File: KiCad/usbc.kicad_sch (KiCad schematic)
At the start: 2 parts, among them J15 JACK-USBE-20PINTL, U9 TPS65987DDKRSHR

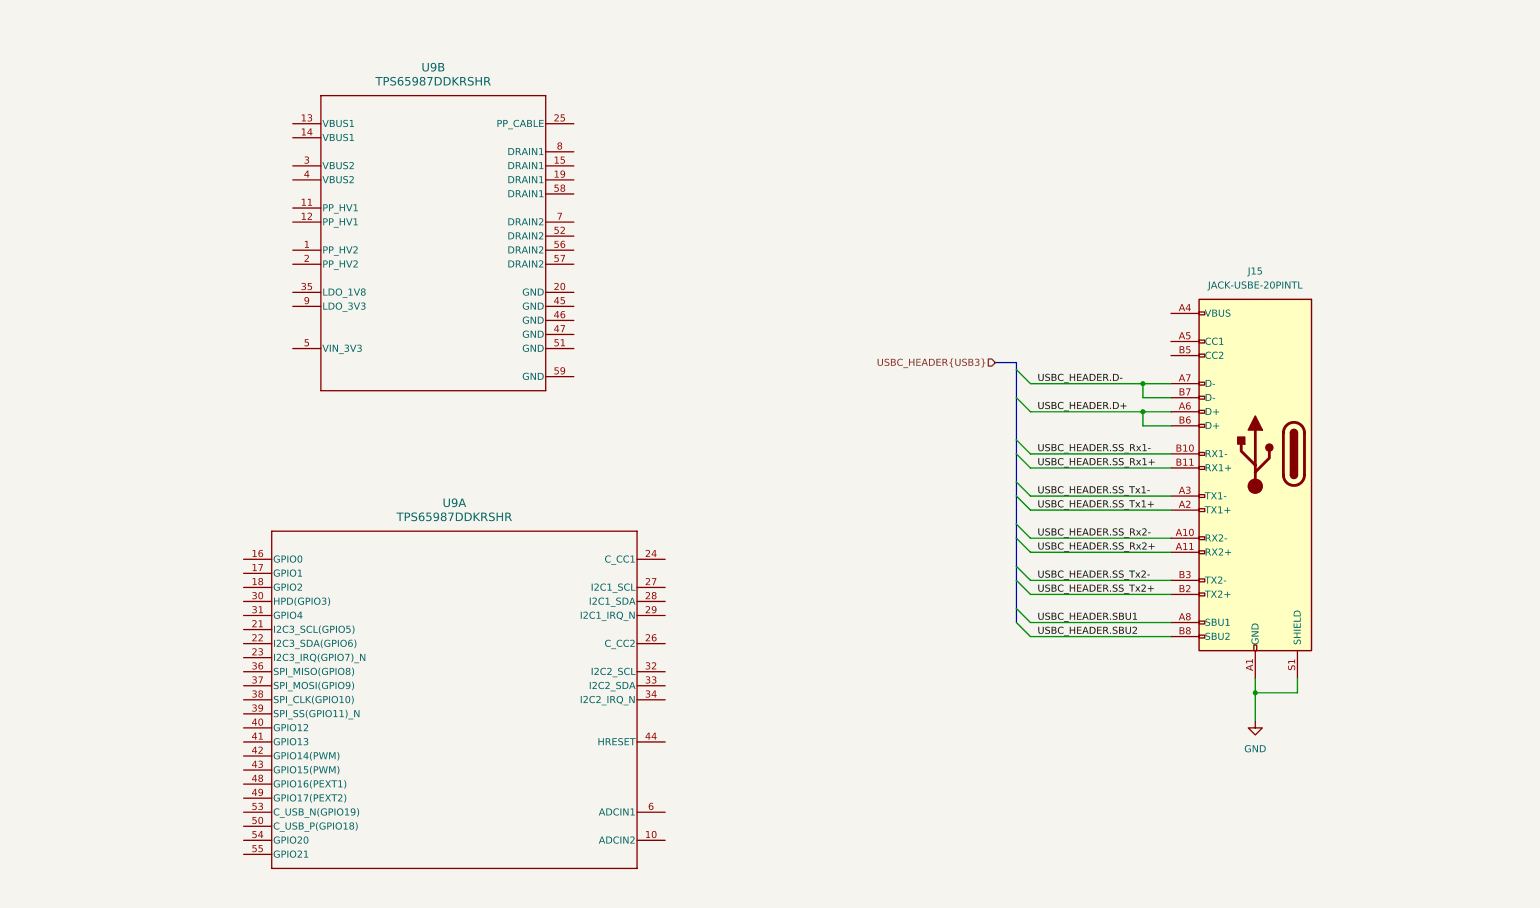
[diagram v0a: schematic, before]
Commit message: Connect TPS65987D I2C and Interrupts
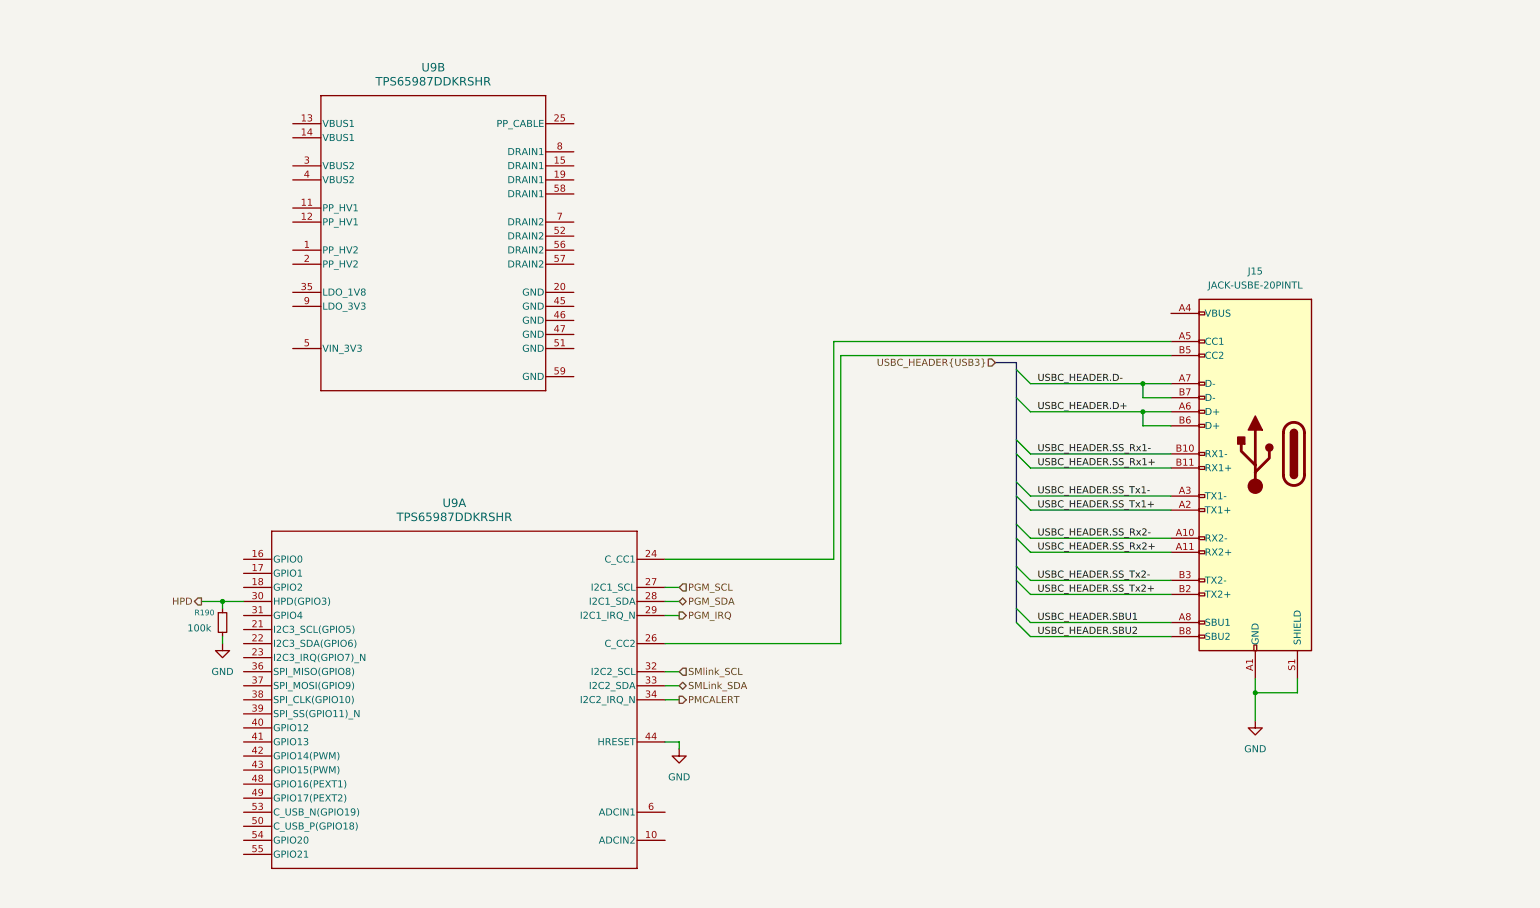
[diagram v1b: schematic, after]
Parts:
- added R190: 100k, symbol Device:R_Small
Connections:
- net GND: now also U9.44 (HRESET), R190.2
- net at J15.A5 (CC1): now also U9.24 (C_CC1)
- net at J15.B5 (CC2): now also U9.26 (C_CC2)
- net PGM_SCL: now reaches U9.27 (I2C1_SCL)
- net PGM_SDA: now reaches U9.28 (I2C1_SDA)
- net PGM_IRQ: now reaches U9.29 (I2C1_IRQ_N)
- net HPD: now reaches U9.30 (HPD(GPIO3))
- net HPD: now also R190.1
- net SMlink_SCL: now reaches U9.32 (I2C2_SCL)
- net SMLink_SDA: now reaches U9.33 (I2C2_SDA)
- net PMCALERT: now reaches U9.34 (I2C2_IRQ_N)

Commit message: Finish wiring TPS65987D
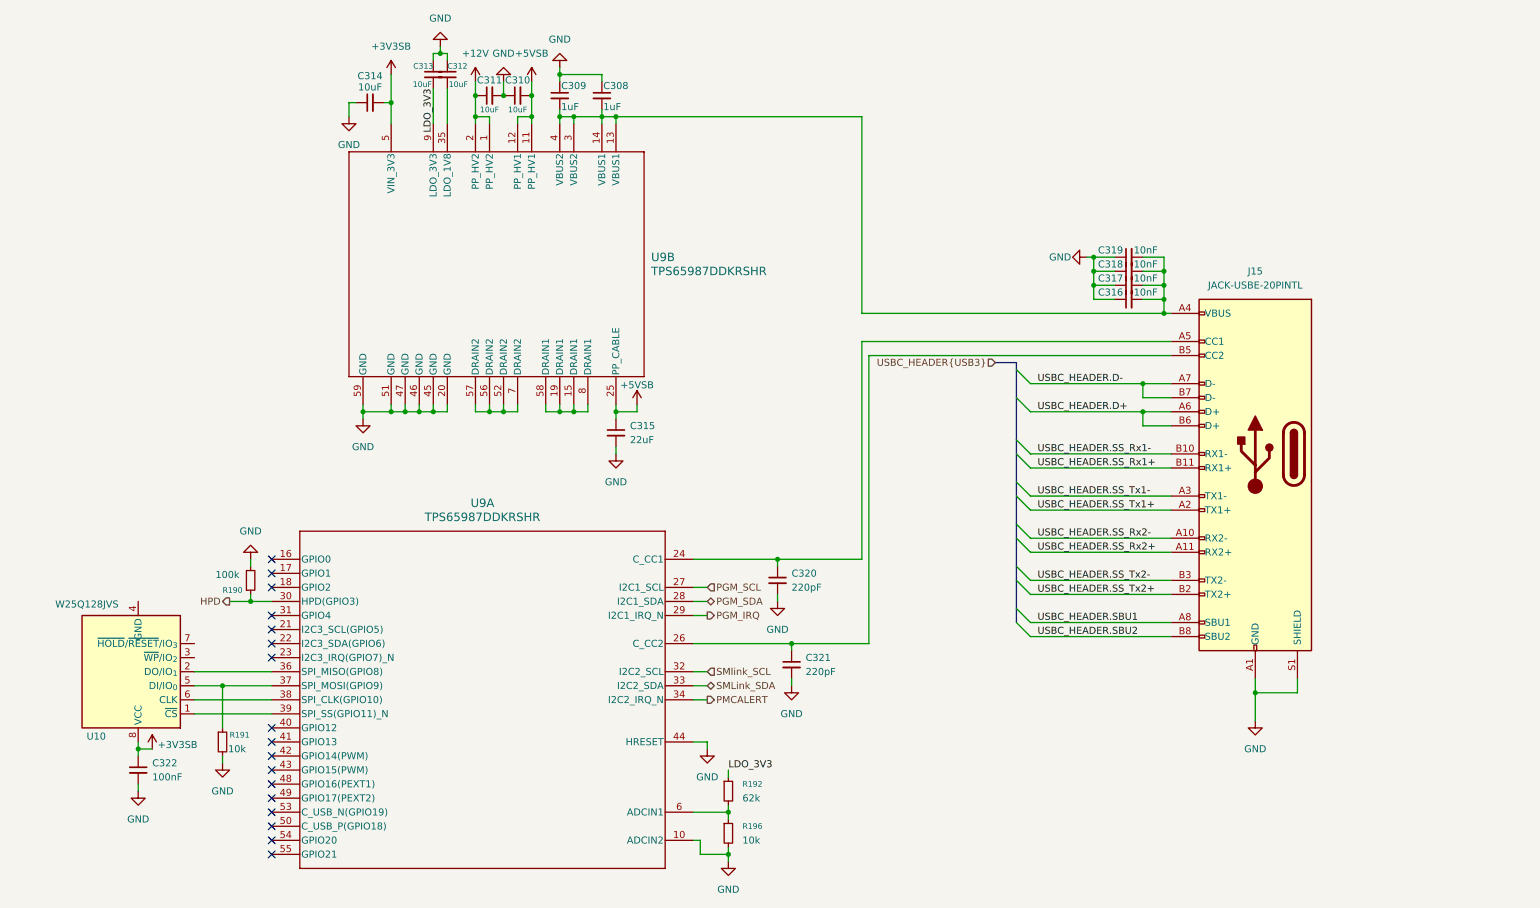
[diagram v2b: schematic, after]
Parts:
- added C308, C309: 1uF, symbol Device:C_Small
- added C310, C311, C312, C313, C314: 10uF, symbol Device:C_Small
- added C315: 22uF, symbol Device:C_Small
- added C316, C317, C318, C319: 10nF, symbol Device:C_Small
- added C320, C321: 220pF, symbol Device:C_Small
- added C322: 100nF, symbol Device:C_Small
- added R191, R196: 10k, symbol Device:R_Small
- added R192: 62k, symbol Device:R_Small
- added U10: W25Q128JVS, Package_SO:SOIC-8_5.3x5.3mm_P1.27mm, symbol Memory_Flash:W25Q128JVS
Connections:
- net GND: now also U9.10 (ADCIN2), U9.20 (GND), U9.45 (GND), U9.46 (GND), U9.47 (GND), U9.51 (GND), U9.59 (GND), C308.1, C309.1, C310.1, C311.2, C312.1, C313.1, C314.1, C315.2, C316.1, C317.1, C318.1, C319.1, C320.2, C321.2, C322.2, R191.2, R196.2
- net at J15.A4 (VBUS), J15.A9 (VBUS), J15.B4 (VBUS)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: now also U9.13 (VBUS1), U9.14 (VBUS1), U9.3 (VBUS2), U9.4 (VBUS2), C308.2, C309.2, C316.2, C317.2, C318.2, C319.2
- net at J15.A5 (CC1), U9.24 (C_CC1): now also C320.1
- net at J15.B5 (CC2), U9.26 (C_CC2): now also C321.1
- net at U9.36 (SPI_MISO(GPIO8)): now also U10.2 (DO/IO_{1})
- net at U9.37 (SPI_MOSI(GPIO9)): now also R191.1, U10.5 (DI/IO_{0})
- net at U9.38 (SPI_CLK(GPIO10)): now also U10.6 (CLK)
- net at U9.39 (SPI_SS(GPIO11)_N): now also U10.1 (~{CS})
- net at U9.6 (ADCIN1): now also R192.2, R196.1
- net +12V: now reaches U9.1 (PP_HV2)
- net +12V: now also U9.2 (PP_HV2), C311.1
- net +5VSB: now reaches U9.11 (PP_HV1)
- net +5VSB: now also U9.12 (PP_HV1), U9.25 (PP_CABLE), C310.2, C315.1
- net at U9.15 (DRAIN1): now also U9.19 (DRAIN1), U9.58 (DRAIN1), U9.8 (DRAIN1)
- net at U9.35 (LDO_1V8): now also C312.2
- net +3V3SB: now reaches U9.5 (VIN_3V3)
- net +3V3SB: now also C314.2, C322.1, U10.8 (VCC)
- net at U9.52 (DRAIN2): now also U9.56 (DRAIN2), U9.57 (DRAIN2), U9.7 (DRAIN2)
- net LDO_3V3: now reaches U9.9 (LDO_3V3)
- net LDO_3V3: now also C313.2, R192.1
- no-connect marks 0 -> 17
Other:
- moved on the sheet: R190, U9A, U9B

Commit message: Fix TPS65987D Symbol
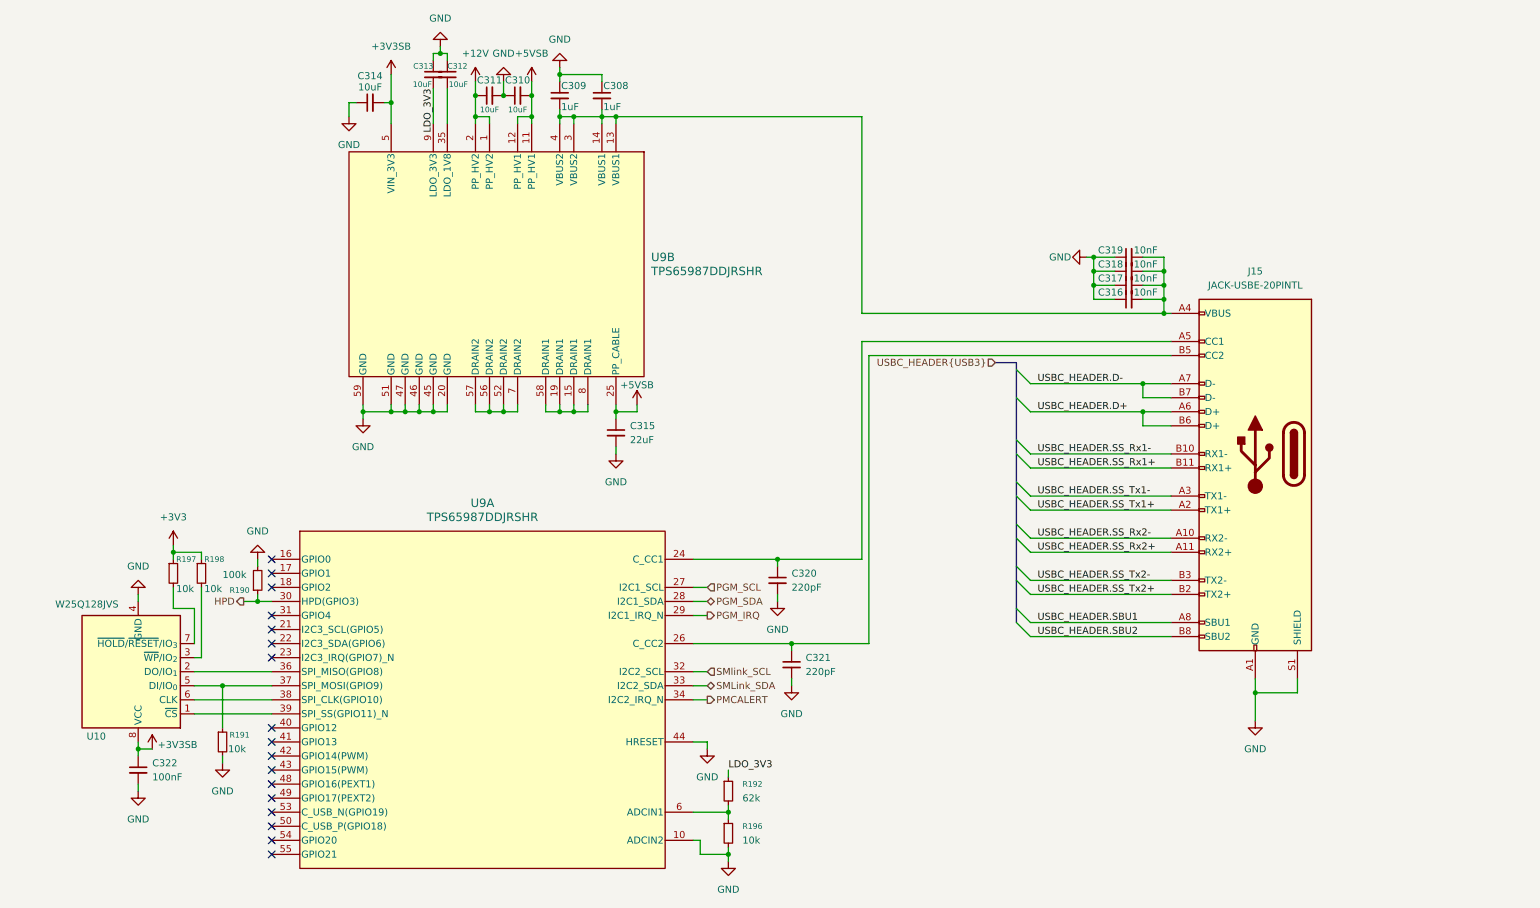
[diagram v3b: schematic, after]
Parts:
- added R197, R198: 10k, symbol Device:R_Small
- U9: value TPS65987DDKRSHR -> TPS65987DDJRSHR
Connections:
- net GND: now also U10.4 (GND)
- net at U10.3 (~{WP}/IO_{2}): now also R198.2
- net at U10.7 (~{HOLD}/~{RESET}/IO_{3}): now also R197.2
- new net +3V3: R197.1, R198.1
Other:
- moved on the sheet: R190

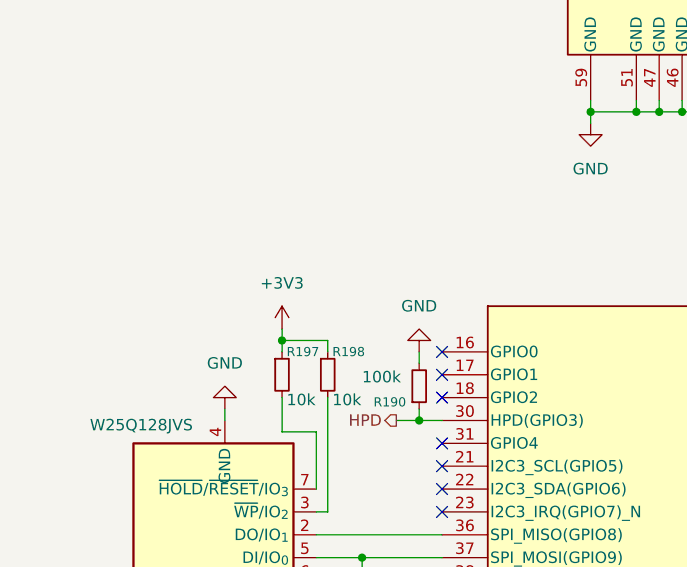
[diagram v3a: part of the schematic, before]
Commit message: Fix some diodes and resistors
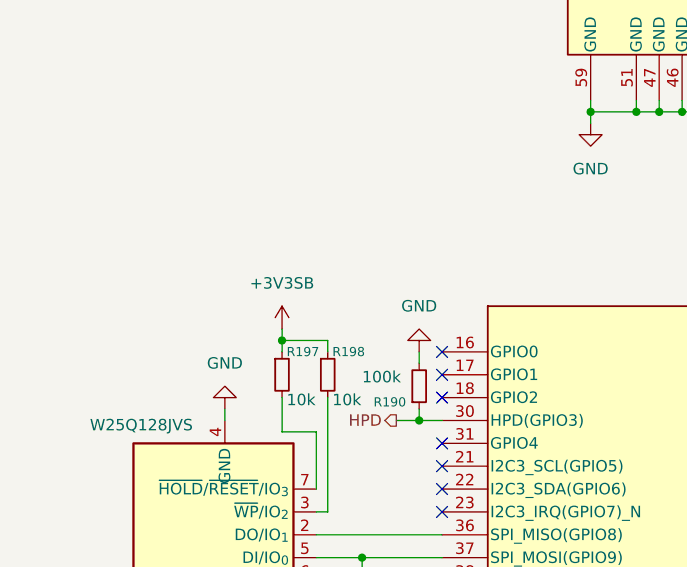
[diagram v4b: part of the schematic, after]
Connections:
- net +3V3 is gone; now on net +3V3SB: R197.1, R198.1
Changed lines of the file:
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@@
 			)
 		)
-		(property "Value" "+3V3"
+		(property "Value" "+3V3SB"
 			(at 35.56 104.14 0)
 			(effects

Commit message: Work though ERC errors
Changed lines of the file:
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@@
 	)
 	(junction
+		(at 123.19 31.75)
+		(diameter 0)
+		(color 0 0 0 0)
+	)
+	(junction
 		(at 214.63 62.23)
 		(diameter 0)
@@
 	(wire
 		(pts
-			(xy 115.57 31.75) (xy 160.02 31.75)
+			(xy 115.57 31.75) (xy 123.19 31.75)
 		)
 		(stroke
@@
 	(wire
 		(pts
+			(xy 123.19 30.48) (xy 123.19 31.75)
+		)
+		(stroke
+			(width 0)
+			(type default)
+		)
+	)
+	(wire
+		(pts
 			(xy 144.78 111.76) (xy 144.78 113.03)
 		)
@@
 	(wire
 		(pts
+			(xy 123.19 31.75) (xy 160.02 31.75)
+		)
+		(stroke
+			(width 0)
+			(type default)
+		)
+	)
+	(wire
+		(pts
 			(xy 190.5 107.95) (xy 215.9 107.95)
 		)
@@
 					(unit 1)
 				)
+			)
+		)
+	)
+	(symbol
+		(lib_id "power:PWR_FLAG")
+		(at 123.19 30.48 0)
+		(unit 1)
+		(exclude_from_sim no)
+		(in_bom yes)
+		(on_board yes)
+		(dnp no)
+		(fields_autoplaced yes)
+		(property "Reference" "#FLG016"
+			(at 123.19 28.575 0)
+			(effects
+				(font
+					(size 1.27 1.27)
+				)
+				(hide yes)
+			)
+		)
+		(property "Value" "PWR_FLAG"
+			(at 123.19 25.4 0)
+			(effects
+				(font
+					(size 1.27 1.27)
+				)
+			)
+		)
+		(property "Footprint" ""
+			(at 123.19 30.48 0)
+			(effects
+				(font
+					(size 1.27 1.27)
+				)
+				(hide yes)
+			)
+		)
+		(property "Datasheet" "~"
+			(at 123.19 30.48 0)
+			(effects
+				(font
+					(size 1.27 1.27)
+				)
+				(hide yes)
+			)
+		)
+		(property "Description" "Special symbol for telling ERC where power comes from"
+			(at 123.19 30.48 0)
+			(effects
+				(font
+					(size 1.27 1.27)
+				)
+				(hide yes)
+			)
+		)
+		(pin "1"
+		)
+		(instances
+			(project ""
+				(path "/49abeb3a-c598-45a3-ba6b-595eb04f17a8/f577f65a-1a1c-4b75-8a85-8871ada08d9d"
+					(reference "#FLG016")
+					(unit 1)
+				)

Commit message: Re-annotate components
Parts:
- renumbered C322 to C332, C314 to C333, C313 to C334, C312 to C335, C311 to C336, C310 to C337, C309 to C338, C308 to C339, C315 to C340, C320 to C341, C321 to C342, C319 to C343, C318 to C344, C317 to C345, C316 to C346, J15 to J26, R197 to R217, R198 to R218, R191 to R219, R190 to R220, R192 to R221, R196 to R222, U10 to U18, U9 to U19

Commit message: Add TVS diodes for ESD protection
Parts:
- added U43, U44: H5VU25U, Package_DFN_QFN:Diodes_UDFN-10_1.0x2.5mm_P0.5mm, symbol Power_Protection:D3V3XA4B10LP
- U18: value W25Q128JVS -> ZD25Q64BSIGT
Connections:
- net GND: now also U43.3 (VSS), U43.8 (VSS), U44.3 (VSS), U44.8 (VSS)
- net USBC_HEADER.SS_Rx1+: now also U43.1
- net USBC_HEADER.SS_Rx1-: now also U43.2
- net USBC_HEADER.SS_Rx2+: now also U44.1
- net USBC_HEADER.SS_Rx2-: now also U44.2
- net USBC_HEADER.SS_Tx1+: now also U43.5
- net USBC_HEADER.SS_Tx1-: now also U43.4
- net USBC_HEADER.SS_Tx2+: now also U44.5
- net USBC_HEADER.SS_Tx2-: now also U44.4
- net +12V renamed +12VCPU
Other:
- moved on the sheet: C343, C344, C345, C346, J26
